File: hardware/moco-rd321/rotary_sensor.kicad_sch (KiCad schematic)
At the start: 2 parts

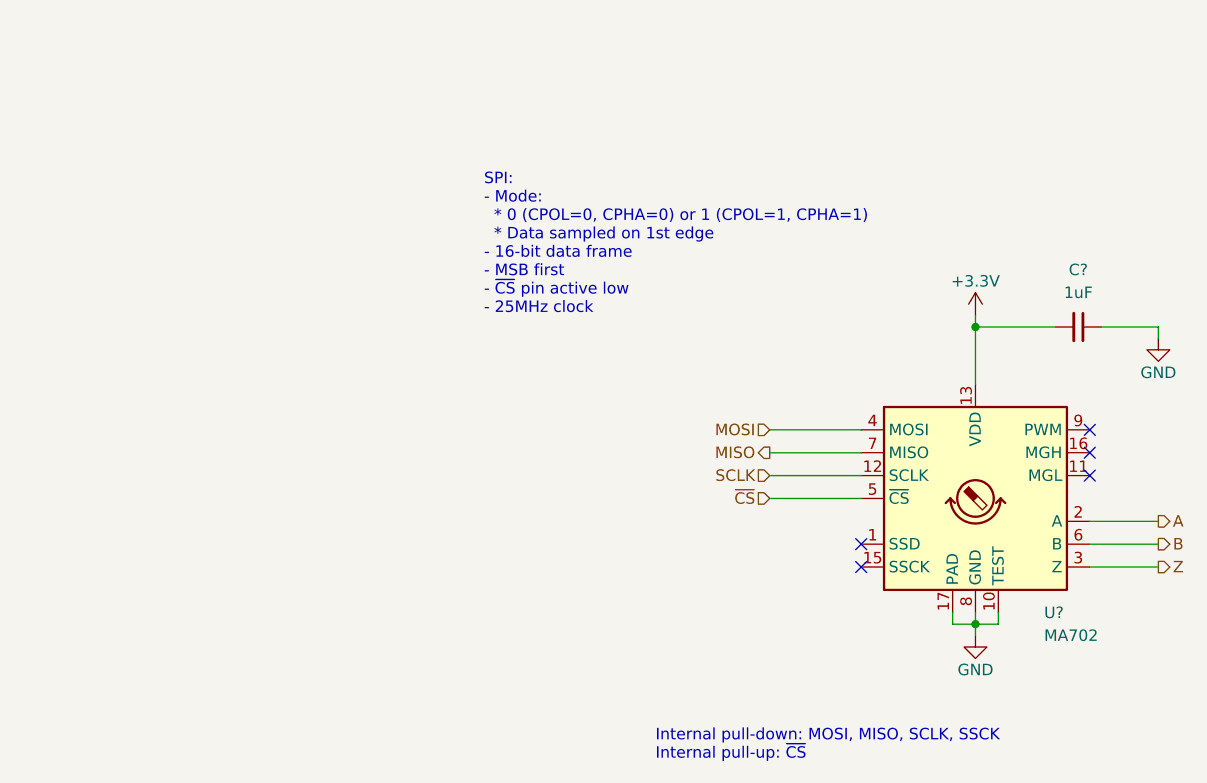
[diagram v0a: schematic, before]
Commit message: Rename RD401 to RD321
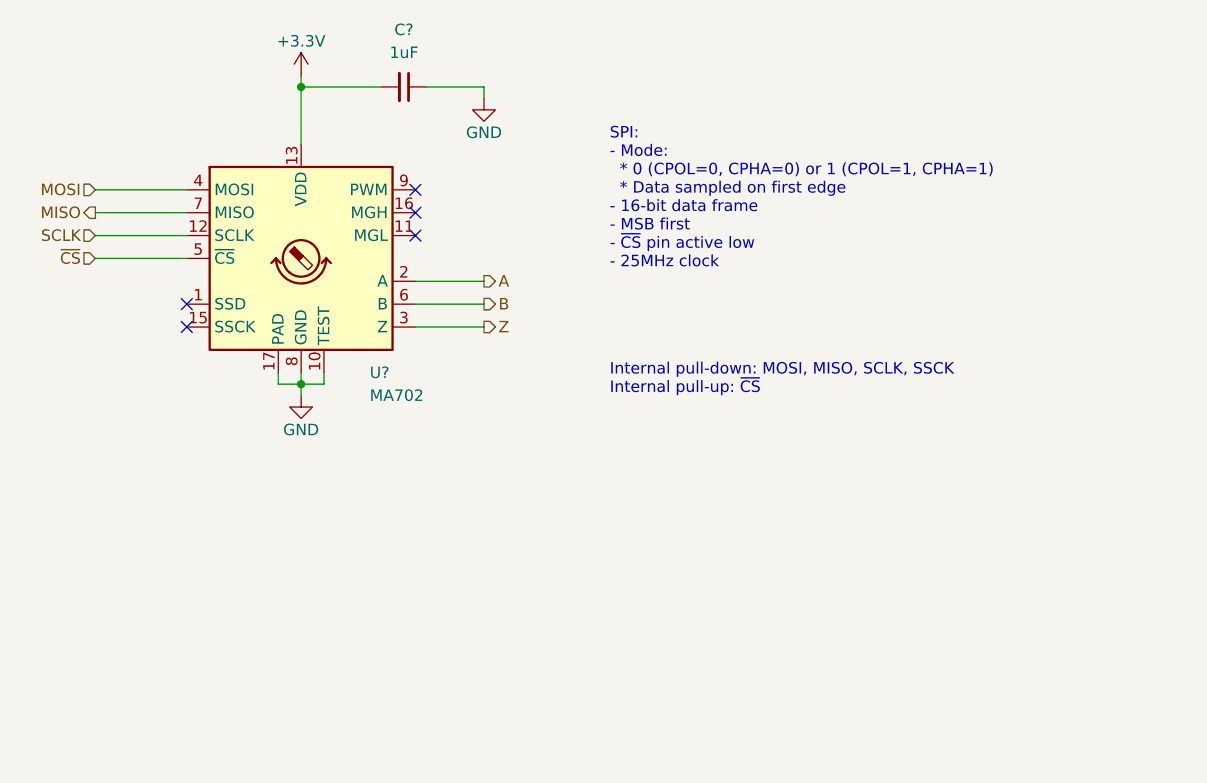
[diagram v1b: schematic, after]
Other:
- note added: "SPI: - Mode: * 0 (CPOL=0, CPHA=0) or 1 (CPOL=1, CPHA=1) * Data sampled on first edge - 16-bit data frame - MSB first - ~{CS} pin active low - 25MHz clock"
- note removed: "SPI: - Mode: * 0 (CPOL=0, CPHA=0) or 1 (CPOL=1, CPHA=1) * Data sampled on 1st edge - 16-bit data frame - MSB first - ~{CS} pin active low - 25MHz clock"
- moved on the sheet: C?, U?
